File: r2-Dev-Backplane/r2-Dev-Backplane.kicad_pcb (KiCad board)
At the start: 4 copper layers, 77.9 x 67.1 mm, 38 parts, among them CON1 USB-MICRO-B, J1 CONN_01X05, J10 Battery SW, J11 OPTS, J2 CONN_01X08, J3 Conn_02x12_Odd_Even, J4 CONN_01X02, J5 CONN_01X08, J7 Li-Po, J8 JTAG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

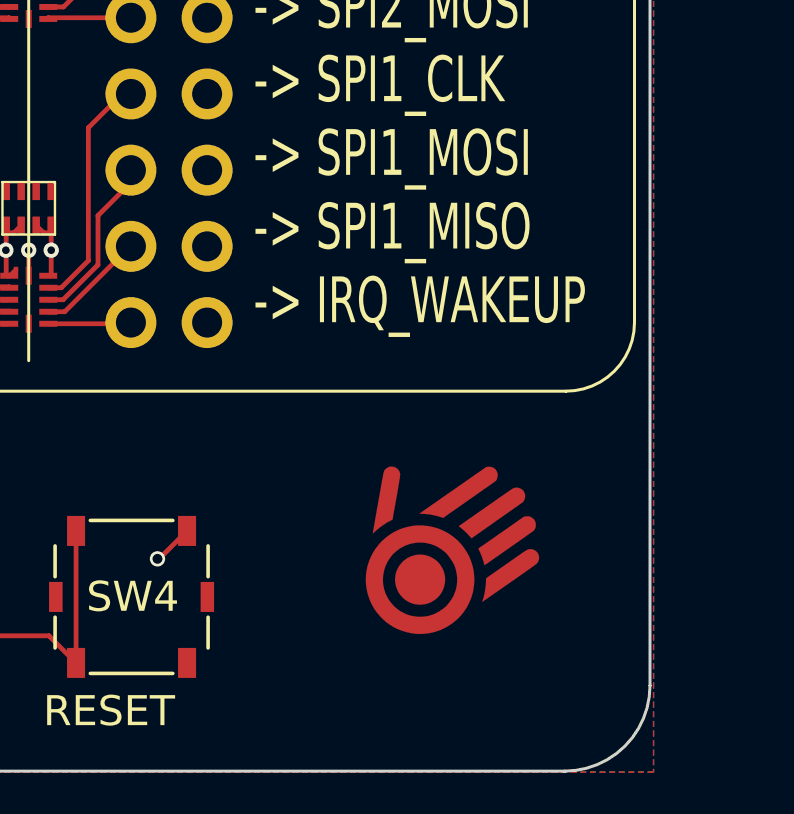
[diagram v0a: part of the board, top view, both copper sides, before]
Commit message: Compute module will now take either WROOM32 module.
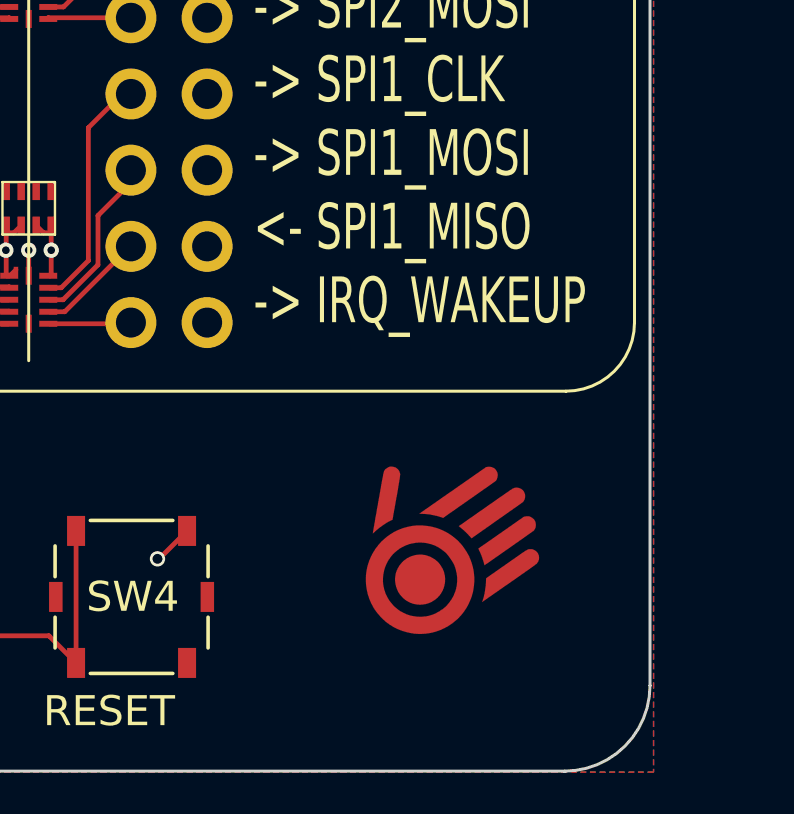
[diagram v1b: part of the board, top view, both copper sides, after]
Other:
- board text added: "-> Batt ~ALERT <- ~LED_RESET -> ~LED_IRQ <- ~REQ -> SPI1_CS <- EXT_CLK <- CPLD_OE <- ~CPLD_RESET -> SPI2_CLK -> SPI2_CS -> SPI2_MOSI -> SPI1_CLK -> SPI1_MOSI <- SPI1_MISO -> IRQ_WAKEUP"
- board text removed: "-> Batt ~ALERT <- ~LED_RESET -> ~LED_IRQ <- ~REQ -> SPI1_CS <- EXT_CLK <- CPLD_OE <- ~CPLD_RESET -> SPI2_CLK -> SPI2_CS -> SPI2_MOSI -> SPI1_CLK -> SPI1_MOSI -> SPI1_MISO -> IRQ_WAKEUP"
